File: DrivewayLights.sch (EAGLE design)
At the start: 61 parts, among them U0 F22X4---DA38, U1 TLC59108PW, U3 A1101, U4 TPS62111RSA

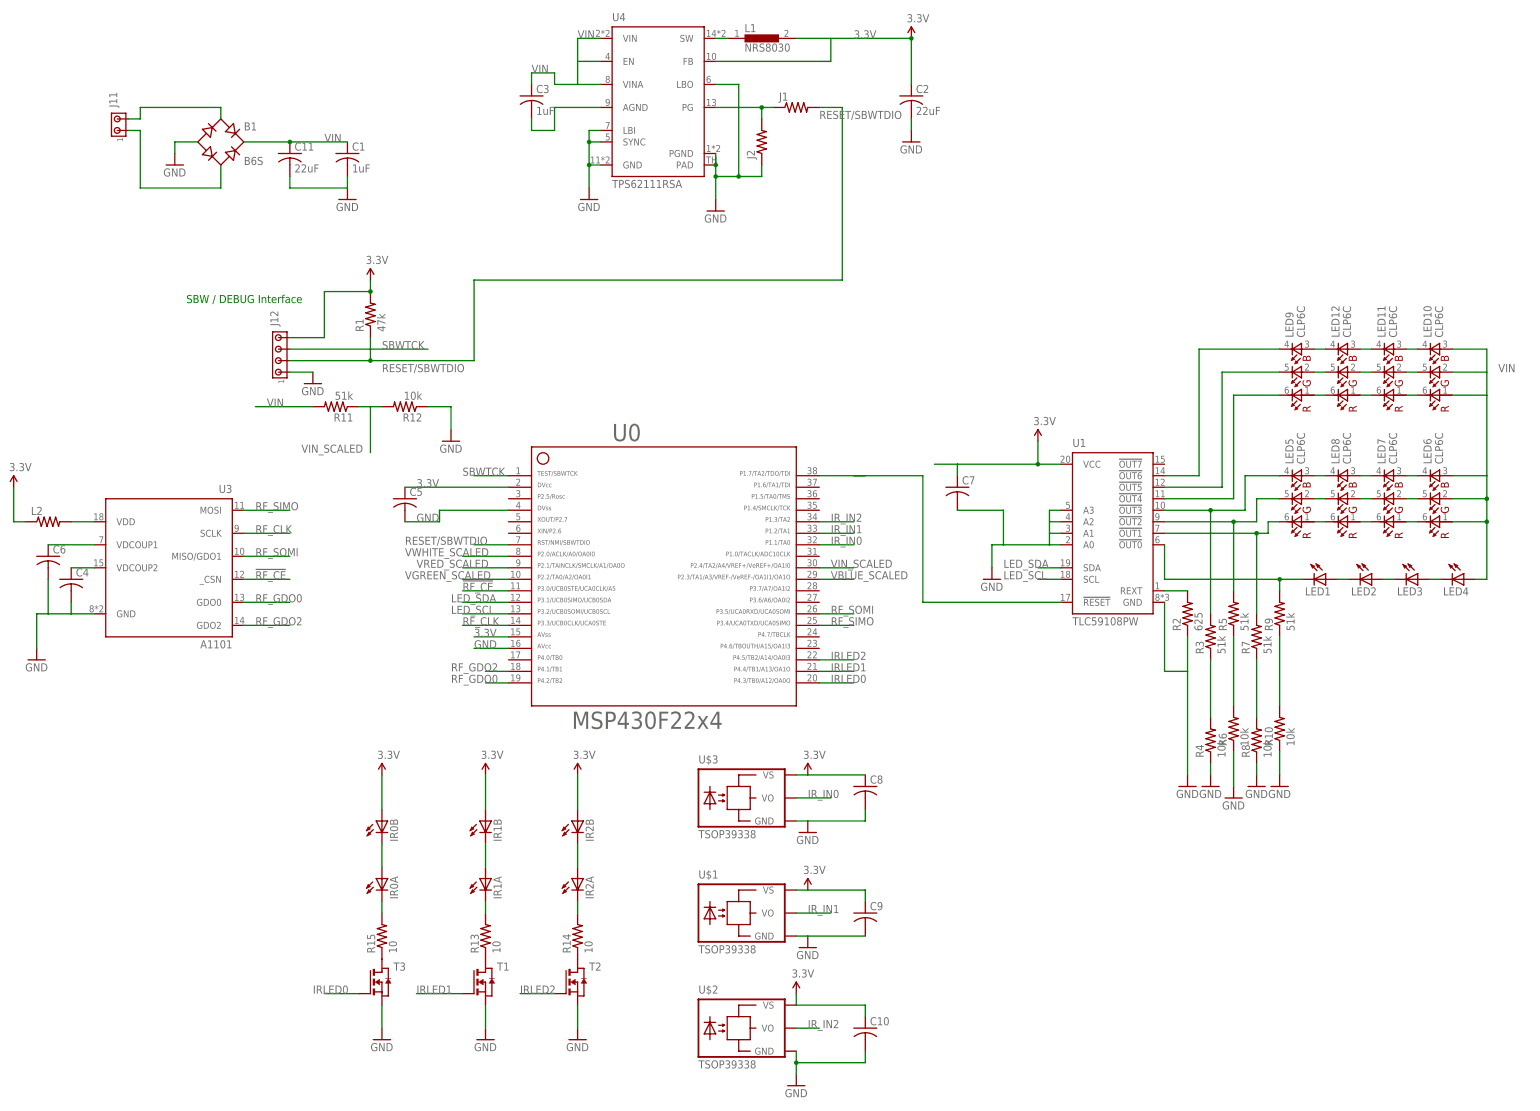
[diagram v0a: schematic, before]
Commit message: First pass at adding the Photon board
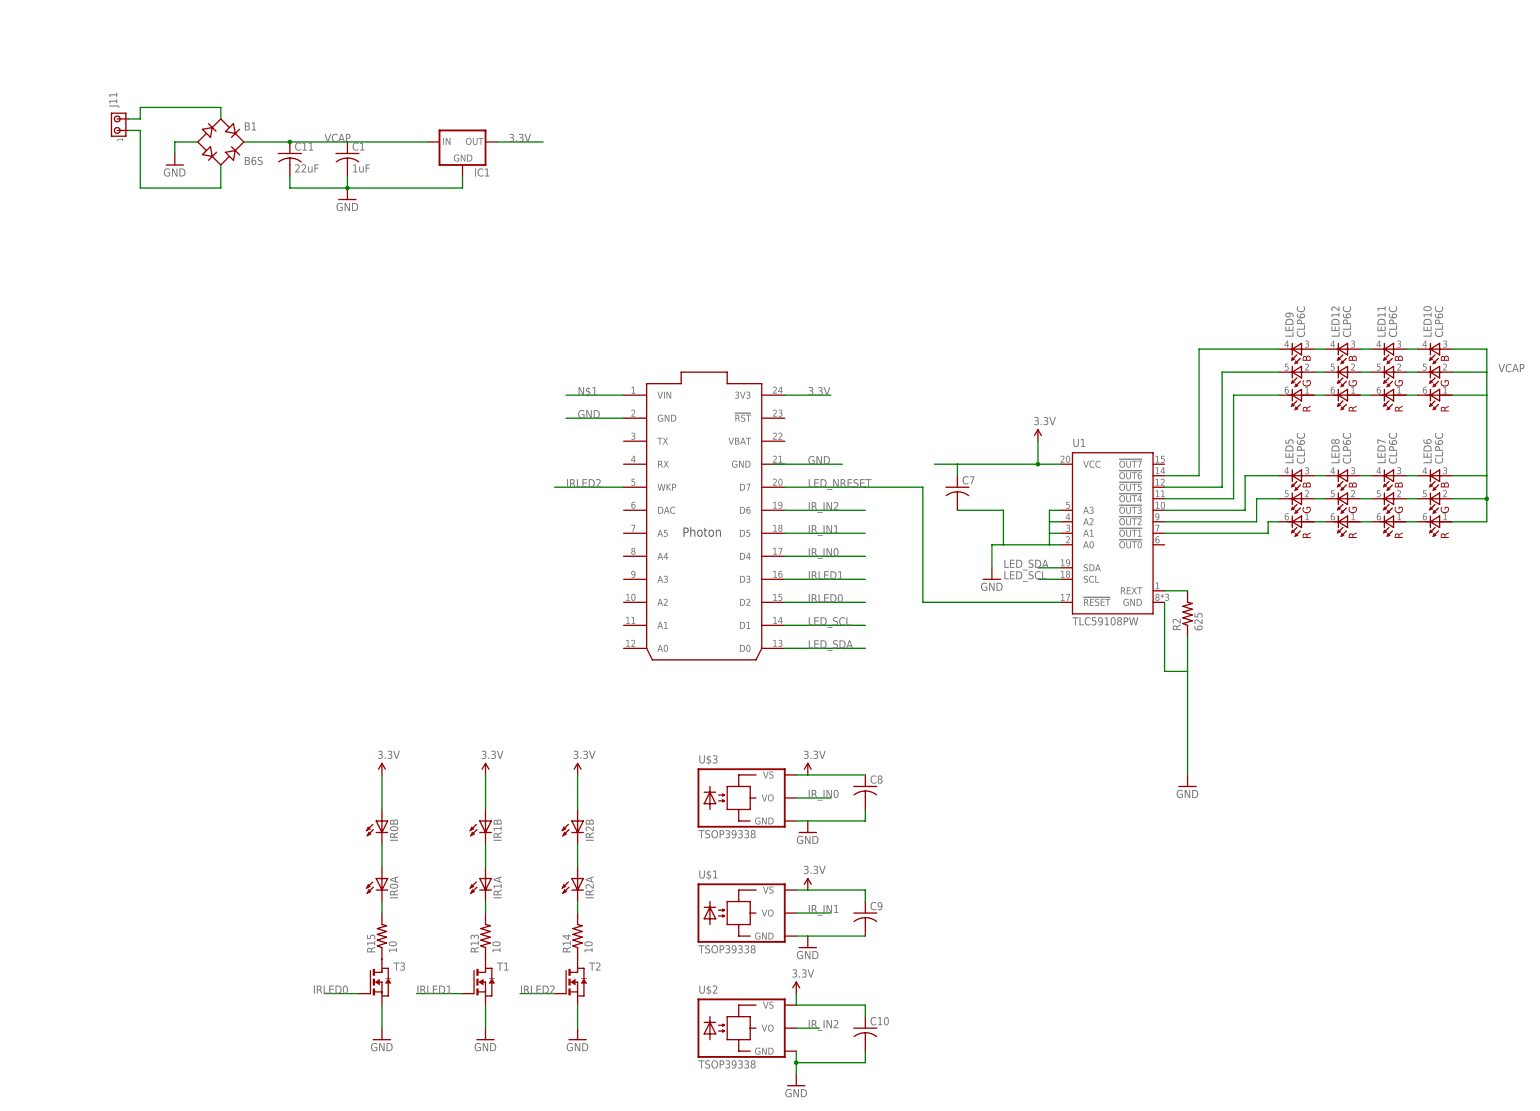
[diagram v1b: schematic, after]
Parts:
- removed C2: 22uF, rcl:C-USC0805
- removed C3: 1uF, rcl:C-USC0603
- removed C4, C5, C6: (no value), rcl:C-USC0603
- removed J1, J2, L2: (no value), rcl:R-US_R0603
- removed J12: (no value), con-amp:MTA04-100
- removed L1: NRS8030, inductors:NRS8030
- removed LED1, LED2, LED3, LED4: (no value), led:LED-2AC-SUPERFLUX
- removed R1: 47k, rcl:R-US_R0603
- removed R10, R12, R4, R6, R8: 10k, rcl:R-US_R0603
- removed R11, R3, R5, R7, R9: 51k, rcl:R-US_R0603
- removed U0: F22X4---DA38, TI_MSP430_v16:F22X4---DA38
- removed U3: A1101, anaren:A1101
- removed U4: TPS62111RSA, texas2:TPS62111RSA
- added IC1: (no value), v-reg:78XXS
- added U2: PHOTON_SMD, Spark:PHOTON_SMD
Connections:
- net N$19 renamed LED_CURRENT_R
- removed net !RF_CE: U0.11, U3._CSN
- removed net N$10: LED1.C, R9.2, U1.!OUT0
- removed net N$34: LED1.A, LED2.C
- removed net N$35: LED2.A, LED3.C
- removed net N$36: LED3.A, LED4.C
- removed net N$38: U1.!RESET
- removed net N$42: L2.2, U3.VDD
- removed net N$7: U0.38
- removed net N$8: C3.2, U4.AGND
- removed net PG: J1.1, J2.2, U4.PG
- removed net RESET/SBWTDIO: J1.2, J12.2, R1.1, U0.7
- removed net RF_CLK: U0.14, U3.SCLK
- removed net RF_GDO0: U0.19, U3.GDO0
- removed net RF_GDO2: U0.18, U3.GDO2
- removed net RF_SIMO: U0.25, U3.MOSI
- removed net RF_SOMI: U0.26, U3.MISO/GDO1
- removed net SBWTCK: J12.3, U0.1
- removed net VBLUE_SCALED: R3.1, R4.2, U0.29
- removed net VDCOUP1: C6.1, U3.VDCOUP1
- removed net VDCOUP2: C4.1, U3.VDCOUP2
- removed net VGREEN_SCALED: R5.1, R6.2, U0.10
- removed net VIN: B1.+, C1.1, C11.1, C3.1, LED10.BA, LED10.GA, LED10.RA, LED4.A, LED6.BA, LED6.GA, LED6.RA, R11.2, U4.EN, U4.VIN, U4.VINA
- removed net VIN_SCALED: R11.1, R12.2, U0.30
- removed net VRED_SCALED: R7.1, R8.2, U0.9
- removed net VWHITE_SCALED: R10.2, R9.1, U0.8
- new net LED_NRESET: U1.!RESET, U2G$1.D7
- new net VCAP: B1.+, C1.1, C11.1, IC1.IN, LED10.BA, LED10.GA, LED10.RA, LED6.BA, LED6.GA, LED6.RA
- net 3.3V: now also IC1.OUT, U2G$1.3V3; no longer C2.1, C5.1, J12.4, L1.2, L2.1, R1.2, U0.15, U0.2, U4.FB
- net BLUE: no longer R3.2
- net GND: now also IC1.GND, U2G$1.GND@2; no longer C2.2, C4.2, C5.2, C6.2, J12.1, J2.1, R10.1, R12.1, R4.1, R6.1, R8.1, U0.16, U0.4, U3.GND, U4.GND, U4.LBI, U4.LBO, U4.PAD, U4.PGND, U4.SYNC
- net GREEN: no longer R5.2
- net IRLED0: now also U2G$1.D2; no longer U0.20
- net IRLED1: now also U2G$1.D3; no longer U0.21
- net IRLED2: now also U2G$1.WKP; no longer U0.22
- net IR_IN0: now also U2G$1.D4; no longer U0.32
- net IR_IN1: now also U2G$1.D5; no longer U0.33
- net IR_IN2: now also U2G$1.D6; no longer U0.34
- net LED_SCL: now also U2G$1.D1; no longer U0.13
- net LED_SDA: now also U2G$1.D0; no longer U0.12
- net N$1: now also U2G$1.VIN; no longer L1.1, U4.SW
- net RED: no longer R7.2
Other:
- note removed: "SBW / DEBUG Interface"

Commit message: Changed to using ESP8266 board and started laying out board.
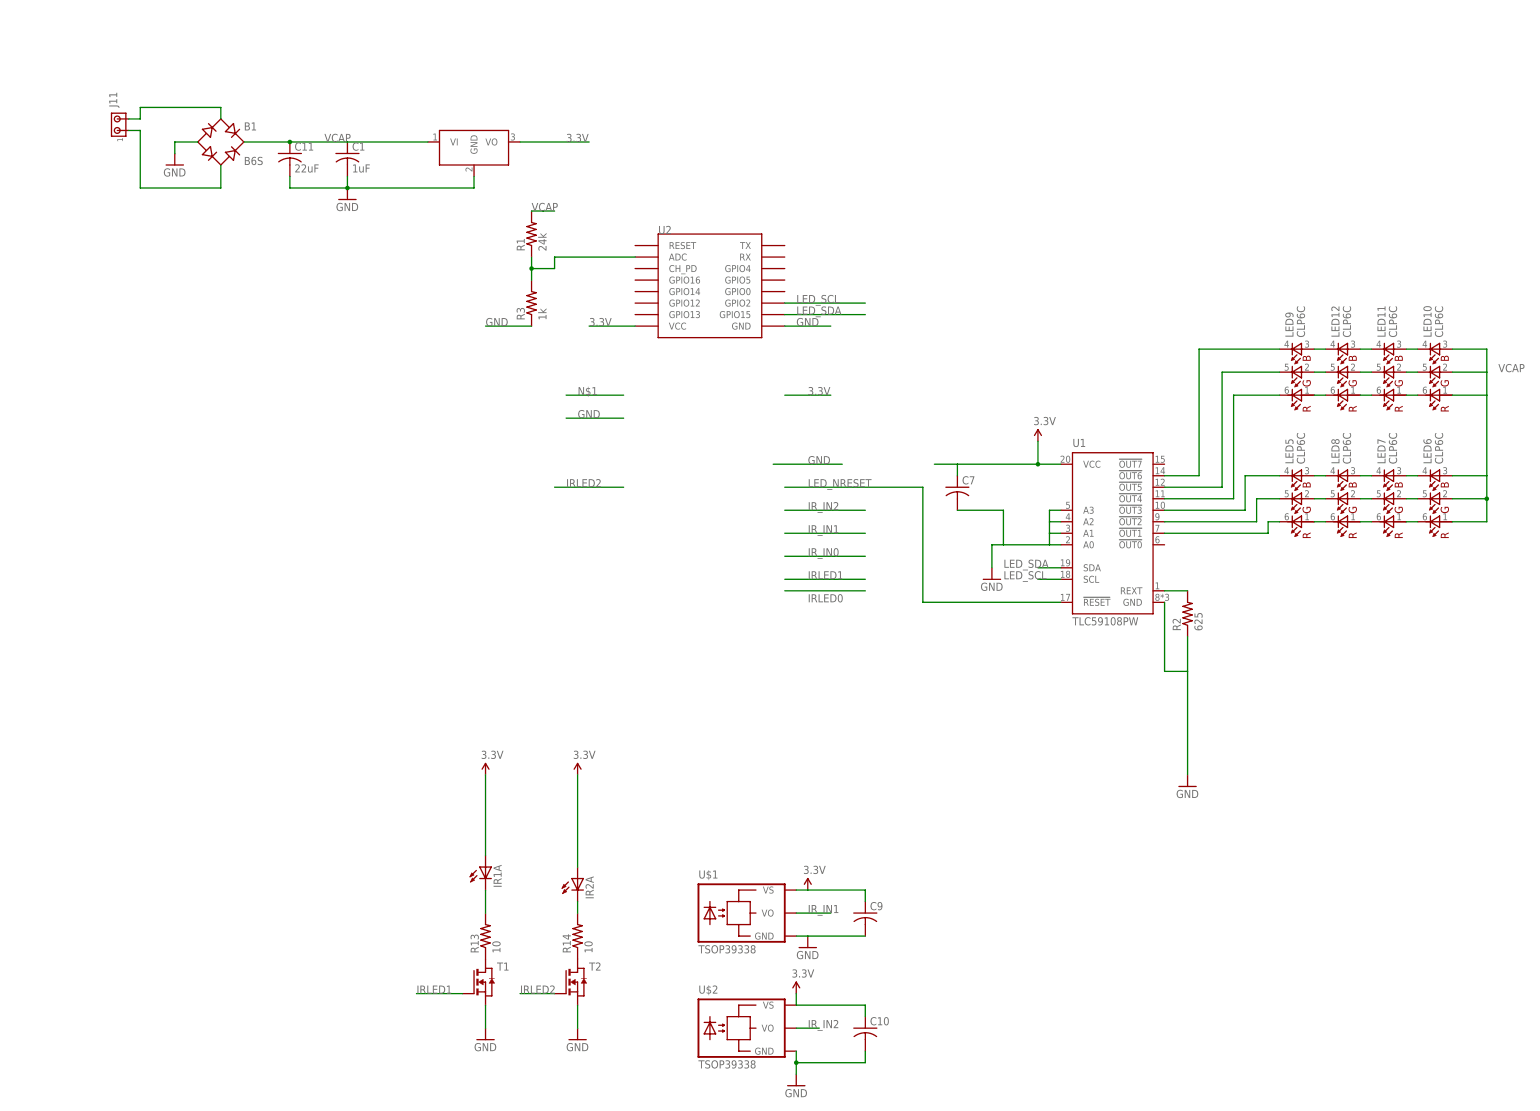
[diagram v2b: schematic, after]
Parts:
- removed C8: (no value), rcl:C-USC0603
- removed IC1: (no value), v-reg:78XXS
- removed IR0A, IR0B, IR1B, IR2B: (no value), led:LED5MM
- removed R15: 10, rcl:R-US_R0603
- removed T3: (no value), zetex:NMOSSOT23
- removed U$3: TSOP39338, opto-vishay:TSOP39338
- added R1: 24k, resistor:R-US_R0603
- added R3: 1k, resistor:R-US_R0603
- added U$4: DCDC_OKI-78SR, rwt-library:DCDC_OKI-78SR
- U2: value PHOTON_SMD -> (none); device Spark:PHOTON_SMD -> esp8266modules:ESP12SMD
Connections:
- removed net IRLED0: T3.G, U2G$1.D2
- removed net IR_IN0: U$3.VO, U2G$1.D4
- removed net N$1: U2G$1.VIN
- removed net N$22: IR0A.C, R15.2
- removed net N$23: IR0A.A, IR0B.C
- removed net N$24: R15.1, T3.D
- removed net N$3: IR2A.A, IR2B.C
- removed net N$4: IR1A.A, IR1B.C
- new net N$7: R1.1, R3.2, U2.ADC
- net 3.3V: now also IR1A.A, IR2A.A, U$4.VO, U2.VCC; no longer C8.1, IC1.OUT, IR0B.A, IR1B.A, IR2B.A, U$3.VS, U2G$1.3V3
- net GND: now also R3.1, U$4.GND, U2.GND; no longer C8.2, IC1.GND, T3.S, U$3.GND, U2G$1.GND@2
- net IRLED1: no longer U2G$1.D3
- net IRLED2: no longer U2G$1.WKP
- net IR_IN1: no longer U2G$1.D5
- net IR_IN2: no longer U2G$1.D6
- net LED_NRESET: no longer U2G$1.D7
- net LED_SCL: now also U2.GPIO2; no longer U2G$1.D1
- net LED_SDA: now also U2.GPIO15; no longer U2G$1.D0
- net VCAP: now also R1.2, U$4.VI; no longer IC1.IN
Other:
- moved on the sheet: IR1A

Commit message: Updated to a fully routed board.  Could have some bugs, needs electrical and mechanical review
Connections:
- net IRLED1: now also U2.GPIO12
- net IRLED2: now also U2.GPIO5
- net IR_IN1: now also U2.GPIO13
- net IR_IN2: now also U2.GPIO0
- net LED_NRESET: now also U2.GPIO14
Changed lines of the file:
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@@
-</segment>
-<segment>
-<wire x1="0" y1="27.94" x2="-12.7" y2="27.94" width="0.1524" layer="91"/>
-<label x="-10.16" y="27.94" size="1.778" layer="95"/>
-</segment>
-<segment>
-<wire x1="33.02" y1="17.78" x2="48.26" y2="17.78" width="0.1524" layer="91"/>
-<label x="40.64" y="17.78" size="1.778" layer="95"/>
 </segment>
 <segment>
@@
 </segment>
 <segment>
-<wire x1="35.56" y1="33.02" x2="45.72" y2="33.02" width="0.1524" layer="91"/>
-<label x="40.64" y="33.02" size="1.778" layer="95"/>
-</segment>
-<segment>
 <pinref part="U2" gate="G$1" pin="VCC"/>
 <wire x1="2.54" y1="48.26" x2="-7.62" y2="48.26" width="0.1524" layer="91"/>
@@
 </segment>
 <segment>
-<wire x1="0" y1="12.7" x2="-15.24" y2="12.7" width="0.1524" layer="91"/>
-<label x="-12.7" y="12.7" size="1.778" layer="95"/>
+<pinref part="U2" gate="G$1" pin="GPIO5"/>
+<wire x1="35.56" y1="58.42" x2="50.8" y2="58.42" width="0.1524" layer="91"/>
+<label x="38.1" y="58.42" size="1.778" layer="95"/>
 </segment>
 </net>
@@
 </segment>
 <segment>
-<wire x1="35.56" y1="-7.62" x2="53.34" y2="-7.62" width="0.1524" layer="91"/>
-<label x="40.64" y="-7.62" size="1.778" layer="95"/>
+<pinref part="U2" gate="G$1" pin="GPIO12"/>
+<wire x1="2.54" y1="53.34" x2="-7.62" y2="53.34" width="0.1524" layer="91"/>
+<label x="-7.62" y="53.34" size="1.778" layer="95"/>
 </segment>
 </net>
@@
 </segment>
 <segment>
-<wire x1="35.56" y1="7.62" x2="53.34" y2="7.62" width="0.1524" layer="91"/>
-<label x="40.64" y="7.62" size="1.778" layer="95"/>
+<pinref part="U2" gate="G$1" pin="GPIO0"/>
+<wire x1="35.56" y1="55.88" x2="53.34" y2="55.88" width="0.1524" layer="91"/>
+<label x="38.1" y="55.88" size="1.778" layer="95"/>
 </segment>
 </net>
@@
 </segment>
 <segment>
-<wire x1="35.56" y1="2.54" x2="53.34" y2="2.54" width="0.1524" layer="91"/>
-<label x="40.64" y="2.54" size="1.778" layer="95"/>
-</segment>
-</net>
-<net name="IRLED0" class="0">
-<segment>
-<wire x1="35.56" y1="-10.16" x2="53.34" y2="-10.16" width="0.1524" layer="91"/>
-<label x="40.64" y="-12.7" size="1.778" layer="95"/>
-</segment>
-</net>
-<net name="IR_IN0" class="0">
-<segment>
-<wire x1="35.56" y1="-2.54" x2="53.34" y2="-2.54" width="0.1524" layer="91"/>
-<label x="40.64" y="-2.54" size="1.778" layer="95"/>
+<pinref part="U2" gate="G$1" pin="GPIO13"/>
+<wire x1="2.54" y1="50.8" x2="-7.62" y2="50.8" width="0.1524" layer="91"/>
+<label x="-7.62" y="50.8" size="1.778" layer="95"/>
 </segment>
 </net>
@@
 <pinref part="U1" gate="G$1" pin="!RESET"/>
 <wire x1="96.52" y1="-12.7" x2="66.04" y2="-12.7" width="0.1524" layer="91"/>
-<wire x1="66.04" y1="-12.7" x2="66.04" y2="12.7" width="0.1524" layer="91"/>
-<wire x1="66.04" y1="12.7" x2="35.56" y2="12.7" width="0.1524" layer="91"/>
-<label x="40.64" y="12.7" size="1.778" layer="95"/>
+<label x="66.04" y="-12.7" size="1.778" layer="95"/>
+</segment>
+<segment>
+<pinref part="U2" gate="G$1" pin="GPIO14"/>
+<wire x1="2.54" y1="55.88" x2="-12.7" y2="55.88" width="0.1524" layer="91"/>
+<wire x1="-12.7" y1="55.88" x2="-12.7" y2="58.42" width="0.1524" layer="91"/>
+<label x="-10.16" y="55.88" size="1.778" layer="95"/>
 </segment>
 </net>
@@
 </segment>
 </net>
-<net name="N$1" class="0">
-<segment>
-<wire x1="0" y1="33.02" x2="-12.7" y2="33.02" width="0.1524" layer="91"/>
-<label x="-10.16" y="33.02" size="1.778" layer="95"/>
-</segment>
-</net>
